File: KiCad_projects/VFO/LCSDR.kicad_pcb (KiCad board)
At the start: 2 copper layers, 91 x 77.5 mm, 82 parts, among them J1 SPI, J10 ENCODER, J11 LCD, J12 keyboard, J2 BAND, J3 OUT-TX, J4 UART, J5 PA, J6 12v, J7 OUT 1-120Mhz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

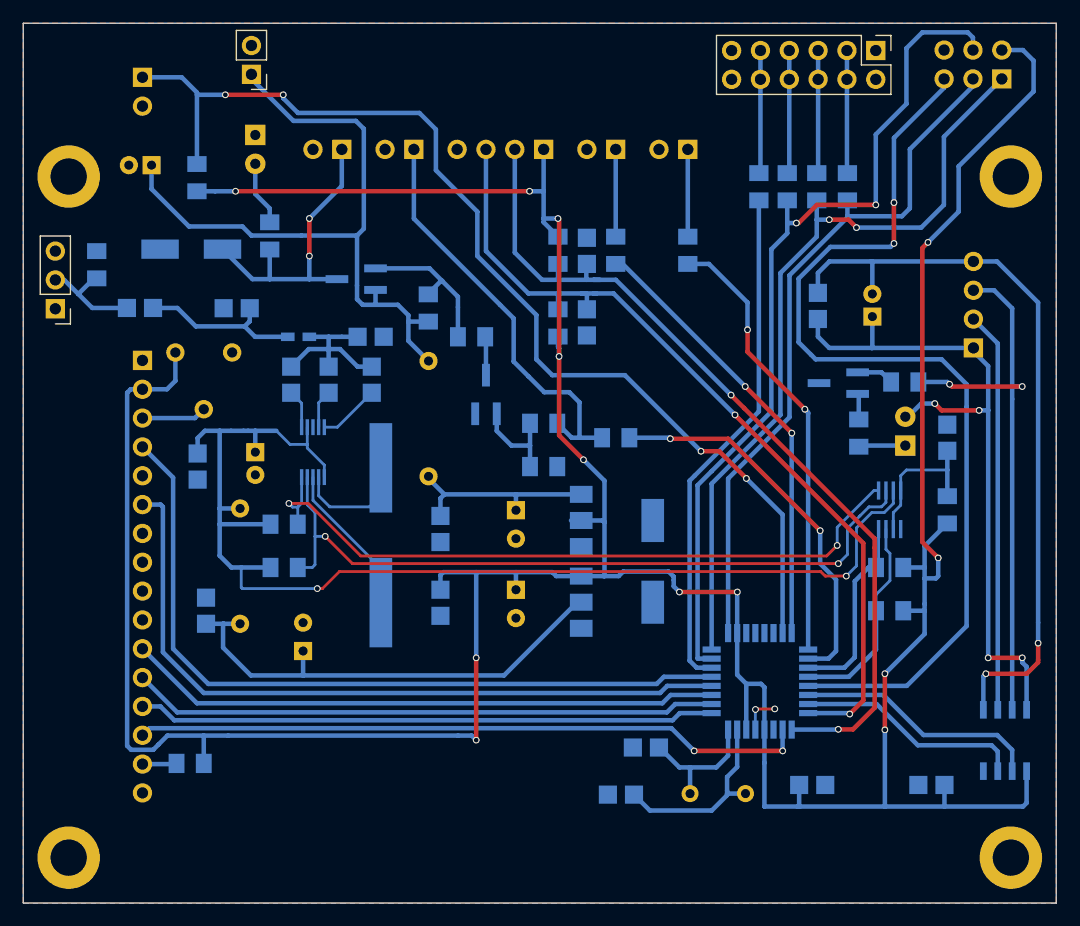
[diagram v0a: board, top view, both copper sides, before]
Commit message: modified VFO schematics and PCB. clk0/clk1/clk2, unified management board
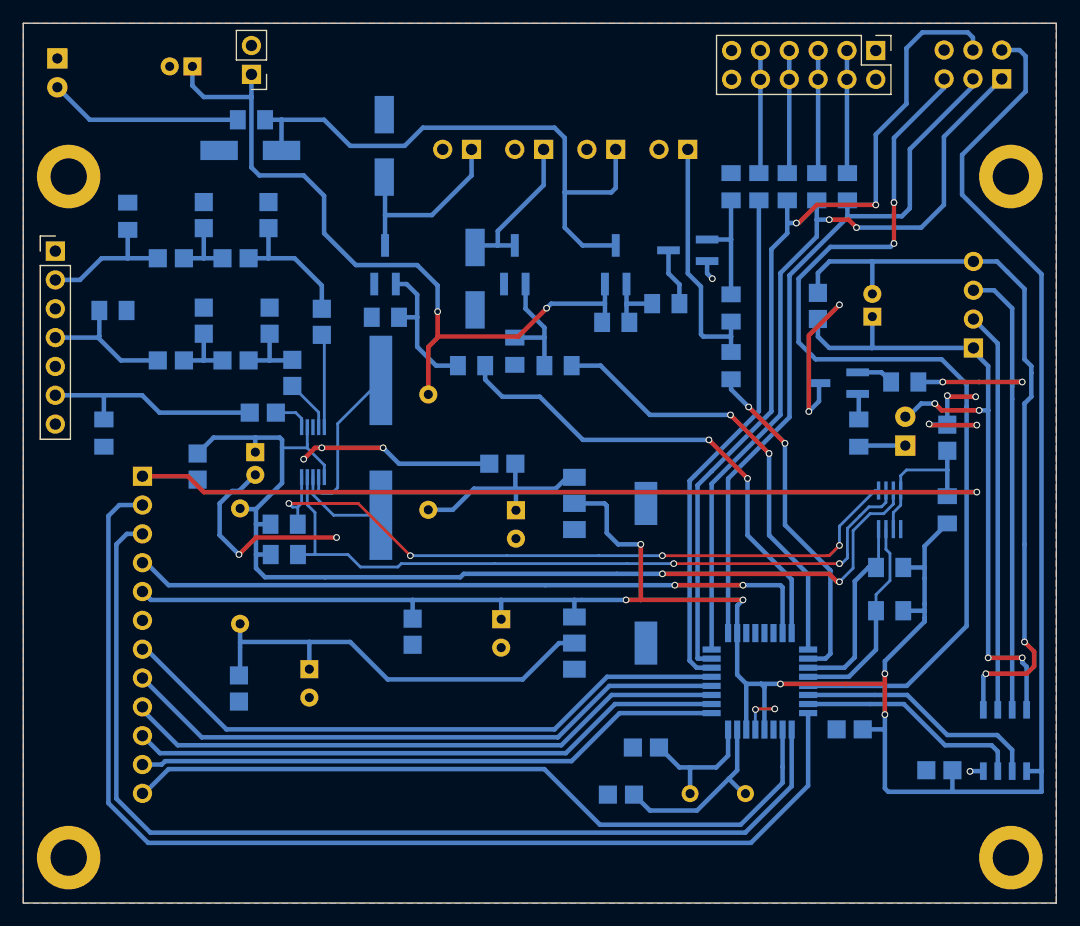
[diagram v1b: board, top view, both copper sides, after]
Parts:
- removed C19, C20: 100nF, LCSDR:C_1206_0603
- removed J11: LCD, Pin_Headers:Pin_Header_Angled_1x16_Pitch2.54mm
- removed P10, P7, P8, P9: CONN_01X01, Mounting_Holes:MountingHole_3.2mm_M3_ISO14580_Pad
- removed RV1: 22k, Potentiometers:Potentiometer_Trimmer_Piher_PT-6v_Horizontal
- added C25: 22pF, LCSDR:C_1206_0603, B.Cu at (86.9, 69.7)
- added C26: 22pF, LCSDR:C_1206_0603, B.Cu at (92.7, 69.7)
- added C28: 10nF, LCSDR:C_1206_0603, B.Cu at (92.1, 77.8)
- added D4: 4148, Diodes_SMD:D_MiniMELF_Handsoldering, B.Cu at (102.8, 54.3)
- added D5: 4148, Diodes_SMD:D_MiniMELF_Handsoldering, B.Cu at (110.8, 66.0)
- added J13: Conn_01x01, Mounting_Holes:MountingHole_3.2mm_M3_DIN965_Pad, F.Cu at (158.0, 57.0)
- added J14: Conn_01x01, Mounting_Holes:MountingHole_3.2mm_M3_DIN965_Pad, F.Cu at (158.0, 117.0)
- added J15: Conn_01x01, Mounting_Holes:MountingHole_3.2mm_M3_DIN965_Pad, F.Cu at (75.0, 117.0)
- added L4: 56nH, LCSDR:C_1206_0603, B.Cu at (89.7, 73.2)
- added Q4: MMBT2222, TO_SOT_Packages_SMD:SOT-23W_Handsoldering, B.Cu at (102.9, 64.8)
- added Q5: MMBT2222, TO_SOT_Packages_SMD:SOT-23W_Handsoldering, B.Cu at (114.3, 64.8)
- C22: value 10nF -> 100nF
- J10: value ENCODER -> MANAGEMENT; footprint Pin_Headers:Pin_Header_Angled_1x04_Pitch2.54mm -> Pin_Headers:Pin_Header_Angled_1x12_Pitch2.54mm
- J12: value keyboard -> Conn_01x01; footprint Pin_Headers:Pin_Header_Angled_1x02_Pitch2.54mm -> Mounting_Holes:MountingHole_3.2mm_M3_DIN965_Pad; moved to F.Cu
- J7: value OUT 1-120Mhz -> OUT; footprint Pin_Headers:Pin_Header_Straight_1x03_Pitch2.54mm -> Pin_Headers:Pin_Header_Straight_1x07_Pitch2.54mm
- L2: footprint Capacitors_SMD:C_0603_HandSoldering -> LCSDR:C_1206_0603
- R17, R18: value 100R -> 1k
- R20: value 15k -> 51R
- R21, R22: value 10k -> 22k
- R23: value 10R -> 51R
- moved J10 45.6 mm to (81.5, 83.4), turned to 180 degrees
- moved R23 30.1 mm to (78.1, 79.6), turned to 270 degrees
- moved R8 29.7 mm to (133.3, 57.9), turned to 90 degrees
- moved J3 24.1 mm to (129.5, 54.6)
- moved J5 24.1 mm to (123.2, 54.6)
- moved Q1 22.9 mm to (123.2, 64.8), turned to 90 degrees
- moved Q2 21.8 mm to (129.5, 63.5), turned to 180 degrees
- moved R7 19.4 mm to (133.3, 68.6), turned to 90 degrees
- moved D1 18.7 mm to (74.0, 46.6)
- moved R16 17.4 mm to (127.6, 68.2)
- moved R2 16.6 mm to (123.2, 69.8), turned to 180 degrees
- moved R21 16.3 mm to (102.9, 69.4), turned to 180 degrees
- moved R17 16.3 mm to (110.5, 73.7), turned to 180 degrees
- moved R18 15.3 mm to (118.1, 73.7), turned to 180 degrees
- moved C22 14.0 mm to (84.0, 73.2), turned to 0 degrees
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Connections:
- C23 pad 1: Net-(C22-Pad1) -> Net-(C23-Pad1)
- C7 pad 1: Net-(C22-Pad1) -> Net-(C7-Pad1)
- C9 pad 1: Net-(C22-Pad1) -> Net-(C7-Pad1)
- J10 pad 1: +5V -> /RESET
- J10 pad 2: Net-(C19-Pad1) -> /ENCODER_B
- J10 pad 3: Net-(C20-Pad1) -> /ENCODER_A
- J10 pad 4: GND -> /KEYBOARD
- J12 pad 1: Net-(J12-Pad1) -> GND
- J8 pad 1: Net-(J8-Pad1) -> Net-(D4-Pad1)
- J9 pad 1: Net-(J9-Pad1) -> Net-(D5-Pad1)
- L2 pad 2: Net-(C22-Pad1) -> Net-(C7-Pad1)
- R17 pad 2: Net-(J8-Pad1) -> Net-(Q4-Pad1)
- R18 pad 2: Net-(J9-Pad1) -> Net-(Q5-Pad1)
- R20 pad 1: Net-(J12-Pad1) -> Net-(C22-Pad1)
- R20 pad 2: +5V -> GND
- R21 pad 1: +5V -> Net-(Q4-Pad1)
- R21 pad 2: Net-(C19-Pad1) -> GND
- R22 pad 1: +5V -> GND
- R22 pad 2: Net-(C20-Pad1) -> Net-(Q5-Pad1)
- R23 pad 1: Net-(J11-Pad15) -> Net-(C28-Pad1)
- R23 pad 2: +5V -> GND
- U1 pad 1: Net-(C19-Pad1) -> /ENCODER_A
- U1 pad 23: Net-(J12-Pad1) -> /KEYBOARD
- U1 pad 32: Net-(C20-Pad1) -> /ENCODER_B
- U2 pad 10: Net-(C23-Pad2) -> Net-(C7-Pad2)
- U2 pad 6: Net-(C7-Pad2) -> Net-(C28-Pad2)
- U2 pad 9: Net-(C22-Pad2) -> Net-(C23-Pad2)
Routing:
- net +5V: track 338.0 -> 221.7 mm, vias 13 -> 6
- net /ENCODER_B: track 0.00 -> 100.3 mm
- net Net-(J12-Pad1): track 96.1 -> 0.00 mm, vias 4 -> 0
- net /ENCODER_A: track 0.00 -> 92.5 mm
- net Net-(C19-Pad1): track 77.7 -> 0.00 mm, vias 2 -> 0
- net Net-(C20-Pad1): track 75.5 -> 0.00 mm, vias 2 -> 0
- net /RESET: track 85.4 -> 160.4 mm, vias 2 -> 3
- net GND: track 3.49 -> 66.8 mm, vias 2 -> 15
- net /KEYBOARD: track 0.00 -> 61.9 mm, vias 0 -> 2
- net Net-(D2-Pad1): track 27.0 -> 52.2 mm, vias 2 -> 0
- net Net-(C28-Pad1): track 0.00 -> 19.9 mm
- net Net-(D4-Pad1): track 0.00 -> 17.4 mm
- net Net-(J3-Pad1): track 37.2 -> 22.2 mm
- net Net-(D5-Pad1): track 0.00 -> 13.7 mm
- net /RS: track 67.9 -> 55.0 mm
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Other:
- board text added: "CLK0"
- board text added: "CLK1"
- board text added: "CLK2"
- board text added: "EXT"
- board text removed: "ENCODER"
- board text removed: "KEYB"
- board text removed: "LCD"

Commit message: Separate boards for VFO, CLK0, CLK1, CLK2 and SWR
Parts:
- added C19: 100nF, LCSDR:C_1206_0603, B.Cu at (96.2, 113.2)
- added C20: 100nF, LCSDR:C_1206_0603, B.Cu at (113.8, 113.2)
- added J11: Conn_01x03, Pin_Headers:Pin_Header_Angled_1x03_Pitch2.54mm, B.Cu at (86.8, 110.5)
- added R25: 2.2k, LCSDR:R_1206_0603, B.Cu at (113.8, 110.0)
- added R26: 2.2k, LCSDR:R_1206_0603, B.Cu at (107.9, 113.2)
- added R27: 2.2k, LCSDR:R_1206_0603, B.Cu at (102.0, 113.2)
- added R28: 2.2k, LCSDR:R_1206_0603, B.Cu at (96.1, 110.0)
- moved U6 0.45 mm to (122.7, 97.7)
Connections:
- U1 pad 19: (no net) -> Net-(C19-Pad2)
- U1 pad 22: (no net) -> Net-(C20-Pad2)
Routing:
- net Net-(C19-Pad2): track 0.00 -> 66.1 mm, vias 0 -> 4
- net Net-(C20-Pad2): track 0.00 -> 48.4 mm, vias 0 -> 2
- net Net-(J11-Pad2): track 0.00 -> 15.9 mm
- net Net-(J11-Pad1): track 0.00 -> 9.74 mm
- net GND: track 66.8 -> 74.3 mm, vias 15 -> 19
- net /ENCODER_A: track 92.5 -> 95.0 mm
- net /ENCODER_B: track 100.3 -> 102.7 mm
- net /DB7: track 65.7 -> 66.5 mm
- net /DB5: track 52.6 -> 51.9 mm
- net /DB4: track 53.5 -> 52.9 mm
- net /E: track 54.2 -> 53.5 mm
- net /RS: track 55.0 -> 54.4 mm
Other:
- board text added: "5v"
- board text added: "A"
- board text added: "B"
- board text added: "DB4"
- board text added: "E"
- board text added: "KEY"
- board text added: "RS"
- board text added: "UT3MK VFO SI5351 v.1.04"
- board text removed: "EXT"

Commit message: Fix some small issues and first tantal release
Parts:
- C10, C11, C3: footprint Capacitors_ThroughHole:CP_Radial_D5.0mm_P2.00mm -> Capacitors_Tantalum_SMD:CP_Tantalum_Case-A_EIA-3216-18_Hand
- C13, C15, C17: footprint Capacitors_ThroughHole:CP_Radial_D6.3mm_P2.50mm -> Capacitors_Tantalum_SMD:CP_Tantalum_Case-D_EIA-7343-31_Hand
- moved C13 7.22 mm to (115.8, 79.3), turned to 180 degrees
- moved C18 5.43 mm to (95.2, 100.7), turned to 180 degrees
- moved C16 5.23 mm to (109.1, 100.7), turned to 180 degrees
- moved C14 4.63 mm to (113.2, 86.9)
- moved C4 4.12 mm to (89.8, 80.3), turned to 180 degrees
- moved C17 3.77 mm to (97.8, 97.0), turned to 180 degrees
- moved C3 3.15 mm to (88.9, 83.2), turned to 180 degrees
- moved C12 2.35 mm to (143.3, 68.2)
- moved C15 2.33 mm to (111.0, 97.0), turned to 180 degrees
- moved C10 1.91 mm to (84.0, 47.5)
- moved C11 1.78 mm to (147.2, 68.3)
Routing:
- net GND: track 74.3 -> 807.8 mm, vias 19 -> 184
- net Net-(C13-Pad1): track 19.0 -> 25.8 mm
- net +5V: track 221.3 -> 228.0 mm
- net Net-(C11-Pad2): track 66.2 -> 59.9 mm
- net Net-(C11-Pad1): track 62.4 -> 56.3 mm
- net /RESET: track 160.4 -> 155.9 mm
- net +3V3: track 39.2 -> 43.6 mm
- net Net-(C3-Pad1): track 95.7 -> 92.3 mm
- net Net-(C19-Pad2): track 66.1 -> 64.9 mm

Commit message: Fix Issues with PCB Silk Text
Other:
- board text added: "REF"
- board text added: "TRNS"
- board text added: "UT3MK VFO SI5351 v.1.05"
- board text removed: "UT3MK VFO SI5351 v.1.04"
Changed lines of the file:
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@@
     (links 199)
     (no_connects 0)
-    (area 70.252381 42.155 165.475001 121.875)
+    (area 70.949999 43.449999 162.050001 121.050001)
     (thickness 1.6)
-    (drawings 32)
+    (drawings 34)
     (tracks 1155)
     (zones 0)
@@
   )
   (layers
-    (0 F.Cu signal)
-    (31 B.Cu signal)
+    (0 F.Cu signal hide)
+    (31 B.Cu signal hide)
     (32 B.Adhes user)
     (33 F.Adhes user)
@@
     )
   )
+  (gr_text REF (at 86.5 107 270) (layer B.SilkS)
+    (effects (font (size 1.5 1.5) (thickness 0.3)) (justify mirror))
+  )
+  (gr_text TRNS (at 89.5 106.5 270) (layer B.SilkS)
+    (effects (font (size 1.5 1.5) (thickness 0.3)) (justify mirror))
+  )
   (gr_text DB4 (at 85.525 103.7 180) (layer B.SilkS)
     (effects (font (size 1.5 1.5) (thickness 0.3)) (justify mirror))
@@
     (effects (font (size 1.5 1.5) (thickness 0.3)) (justify mirror))
   )
-  (gr_text "UT3MK VFO SI5351 v.1.04" (at 135.85 117.75 180) (layer B.SilkS)
+  (gr_text "UT3MK VFO SI5351 v.1.05" (at 135.85 117.75 180) (layer B.SilkS)
     (effects (font (size 1.5 1.5) (thickness 0.3)) (justify mirror))
   )
